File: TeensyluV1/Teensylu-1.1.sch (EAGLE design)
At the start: 101 parts, among them J1 M02POLAR, J11 M02POLAR, J12 M02POLAR, J2 MICROSD, J3 USB-MICRO-PTH, J4 M02POLAR, J5 4P-TERM-BLOCK284391-4, J6 39-29-3066, J7 HOTEND-1, J8 2x7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

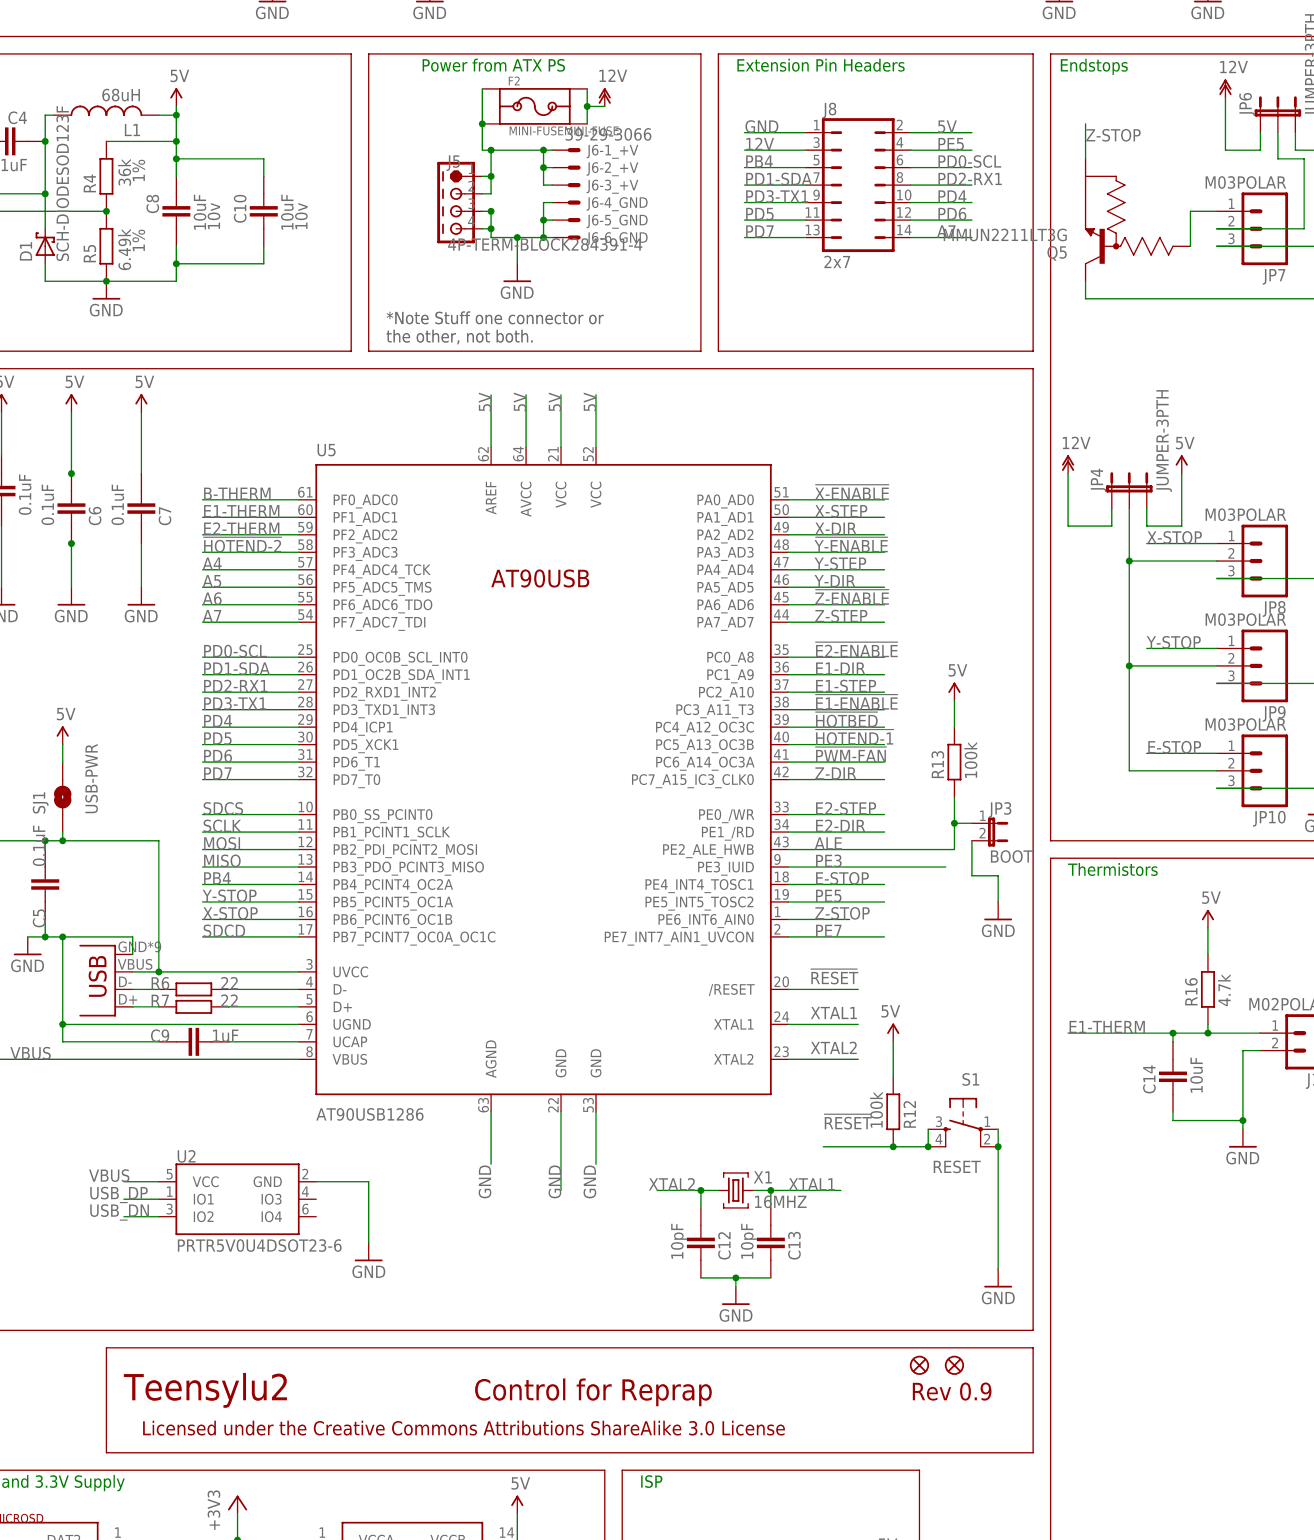
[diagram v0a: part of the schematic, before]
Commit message: Fixed Z endstop
Collector and emitter pins were swapped.
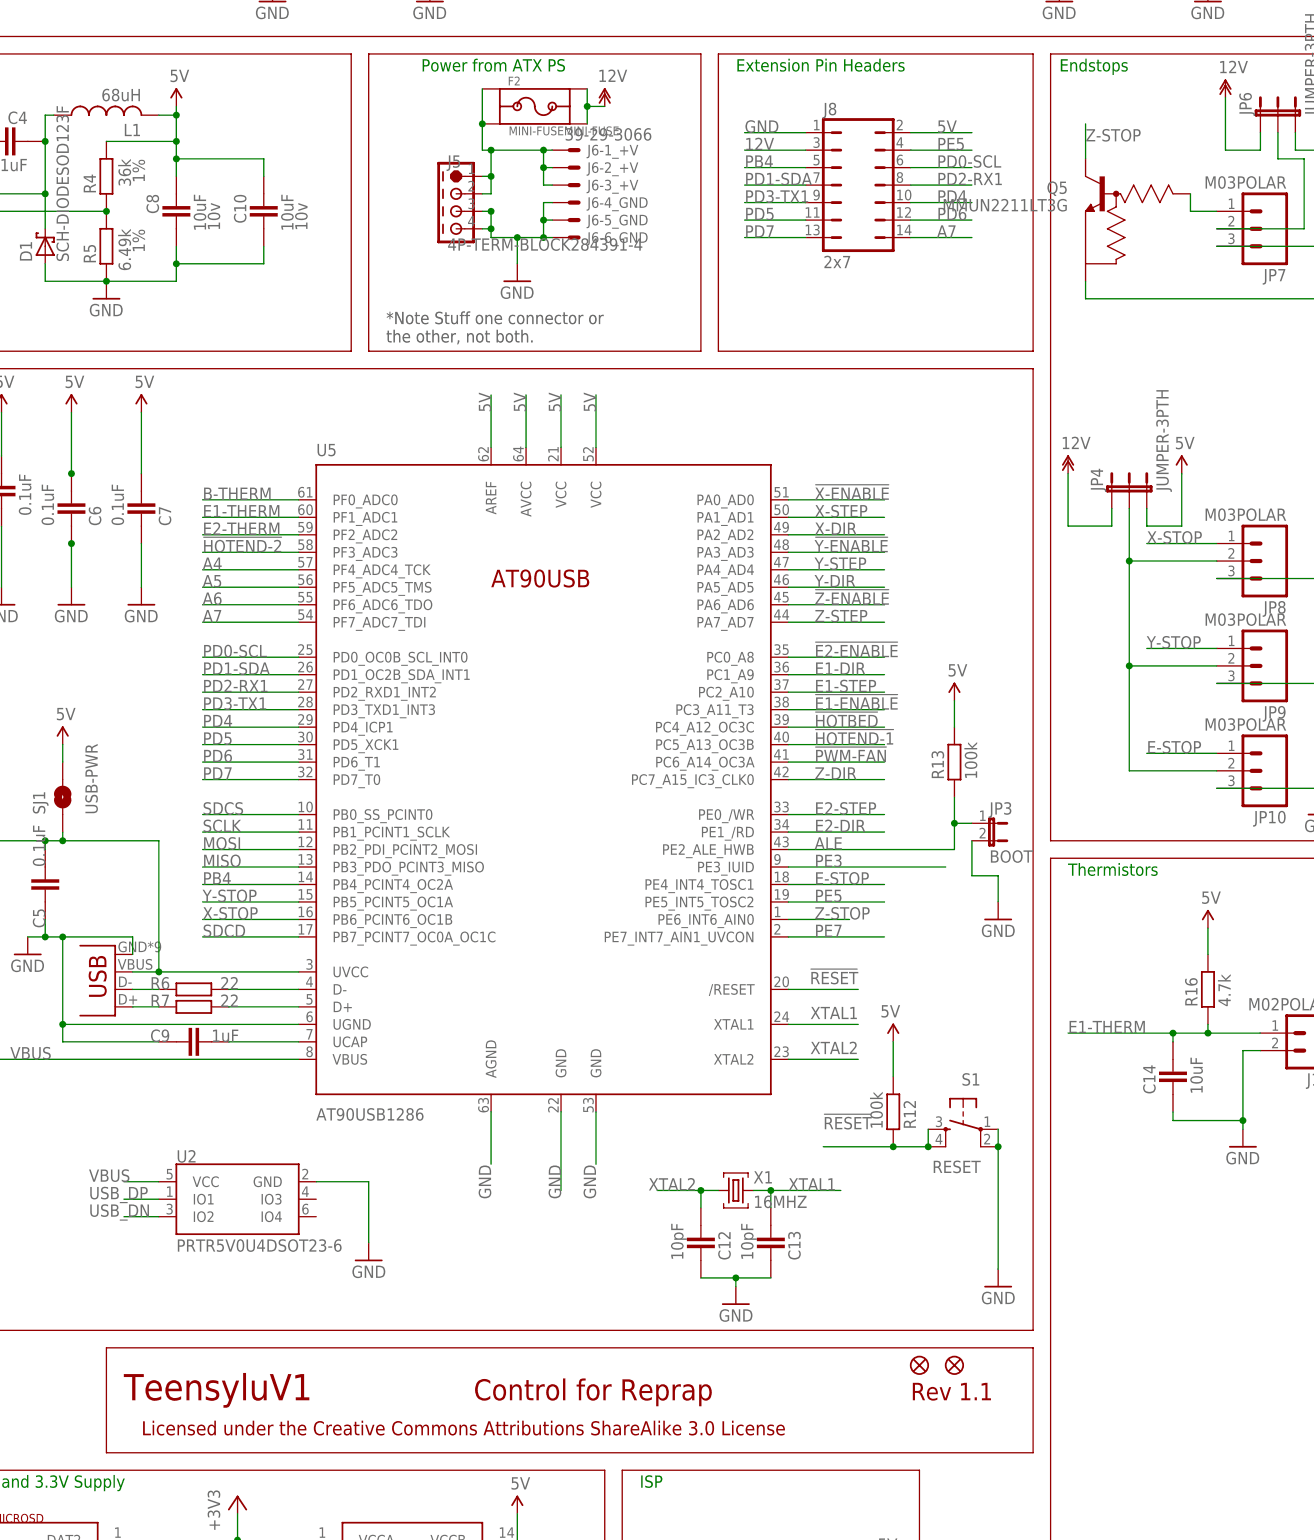
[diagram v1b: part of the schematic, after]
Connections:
- net GND: now also Q5.E; no longer Q5.C
- net Z-STOP: now also Q5.C; no longer Q5.E
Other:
- note added: "Rev 1.1"
- note added: "TeensyluV1"
- note removed: "Rev 0.9"
- note removed: "Teensylu2"
- moved on the sheet: Q5
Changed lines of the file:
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@@
 <text x="1.27" y="238.76" size="1.778" layer="91" font="vector">Mosfets</text>
 <text x="10.16" y="149.86" size="1.778" layer="91" font="vector">Power Acc</text>
-<text x="60.96" y="7.62" size="3.81" layer="94">Teensylu2</text>
-<text x="175.26" y="7.62" size="2.54" layer="94">Rev 0.9</text>
+<text x="60.96" y="7.62" size="3.81" layer="94">TeensyluV1</text>
+<text x="175.26" y="7.62" size="2.54" layer="94">Rev 1.1</text>
 <text x="111.76" y="7.62" size="3.048" layer="94">Control for Reprap</text>
 <text x="63.5" y="2.54" size="2.032" layer="94">Licensed under the Creative Commons Attributions ShareAlike 3.0 License</text>
@@
 <attribute name="NOTES" x="233.68" y="-36.83" size="1.778" layer="96" rot="R180" display="off"/>
 </instance>
-<instance part="Q5" gate="G$1" x="203.2" y="175.26" rot="R180">
-<attribute name="DESCRIPTION" x="203.2" y="175.26" size="1.778" layer="96" rot="R180" display="off"/>
-<attribute name="MANUFACTURER" x="203.2" y="175.26" size="1.778" layer="96" rot="R180" display="off"/>
-<attribute name="MANUFACTURER_PART_NUMBER" x="203.2" y="175.26" size="1.778" layer="96" rot="R180" display="off"/>
+<instance part="Q5" gate="G$1" x="203.2" y="182.88" rot="MR0">
+<attribute name="DESCRIPTION" x="203.2" y="182.88" size="1.778" layer="96" rot="MR0" display="off"/>
+<attribute name="MANUFACTURER" x="203.2" y="182.88" size="1.778" layer="96" rot="MR0" display="off"/>
+<attribute name="MANUFACTURER_PART_NUMBER" x="203.2" y="182.88" size="1.778" layer="96" rot="MR0" display="off"/>
 </instance>
 <instance part="F2" gate="G$1" x="120.65" y="195.58"/>
@@
 <pinref part="JP10" gate="G$1" pin="3"/>
 <junction x="234.95" y="127"/>
-<pinref part="Q5" gate="G$1" pin="C"/>
-<wire x1="200.66" y1="170.18" x2="200.66" y2="167.64" width="0.1524" layer="91"/>
 <wire x1="200.66" y1="167.64" x2="234.95" y2="167.64" width="0.1524" layer="91"/>
 <junction x="234.95" y="167.64"/>
+<pinref part="Q5" gate="G$1" pin="E"/>
+<wire x1="200.66" y1="170.18" x2="200.66" y2="167.64" width="0.1524" layer="91"/>
 </segment>
 <segment>
@@
 <net name="Z-STOP" class="0">
 <segment>
-<pinref part="Q5" gate="G$1" pin="E"/>
-<wire x1="200.66" y1="187.96" x2="200.66" y2="193.04" width="0.1524" layer="91"/>
 <label x="200.66" y="190.5" size="1.778" layer="95"/>
+<pinref part="Q5" gate="G$1" pin="C"/>
+<wire x1="200.66" y1="193.04" x2="200.66" y2="187.96" width="0.1524" layer="91"/>
 </segment>
 <segment>
@@
 <pinref part="JP7" gate="G$1" pin="1"/>
 <pinref part="Q5" gate="G$1" pin="B"/>
-<wire x1="215.9" y1="180.34" x2="215.9" y2="175.26" width="0.1524" layer="91"/>
-</segment>
-</net>
+<wire x1="215.9" y1="180.34" x2="215.9" y2="182.88" width="0.1524" layer="91"/>
+</segment>
+</net>
